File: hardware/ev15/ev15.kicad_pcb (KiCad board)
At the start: 4 copper layers, 94.4 x 80 mm, 165 parts, among them CN1 Conn_05x02_Female, CN2 PJ-242, J1 USB_C_Receptacle, J10 Conn_02x04_Odd_Even, J11 Conn_02x05_Counter_Clockwise, J2 Conn_01x02_Socket, J3 AudioJack4, J4 Conn_01x18_MountingPin, J5 Conn_02x03_Odd_Even, J7 Conn_02x05_Counter_Clockwise, J8 Conn_02x05_Counter_Clockwise, J9 Conn_02x05_Counter_Clockwise, Q1 2N7002, SW1 SW_SPDT, SW2 SW_Push, SW3 SW_Push, SW4 SW_Push, SW5 SW_Push, U1 BQ21040DBV, U10 STM32F405RGTx, U2 USBLC6-2P6, U3 STM32F072CBTx, U4 CH340C, U5 TPS63060, U6 WM8960CGEFL/RV, U7 ESP32-S3-WROOM-1, U8 M24C02-RMN6TP, U9 BM14B(0.8)-24DS-0.4V(53), Y1 Crystal_GND24

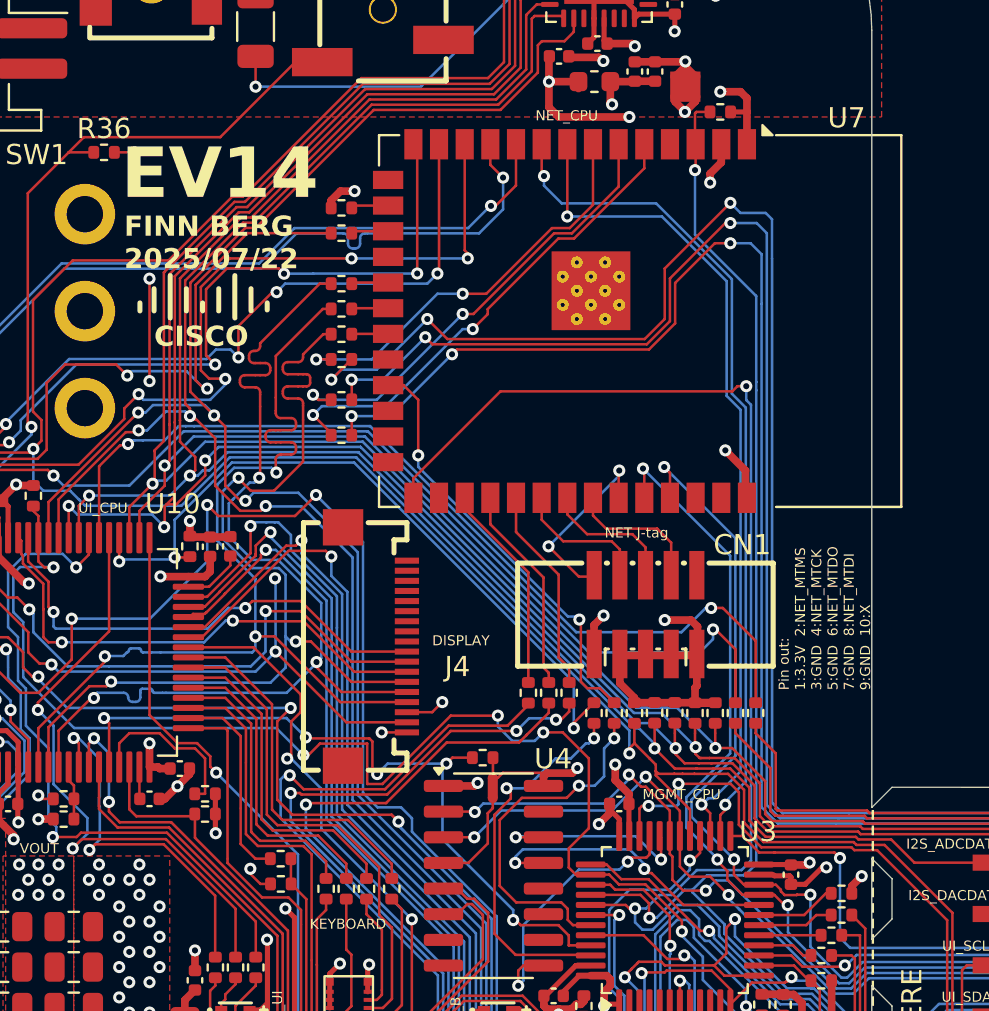
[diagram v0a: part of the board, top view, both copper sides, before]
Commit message: chore: renamed ev14a to ev15
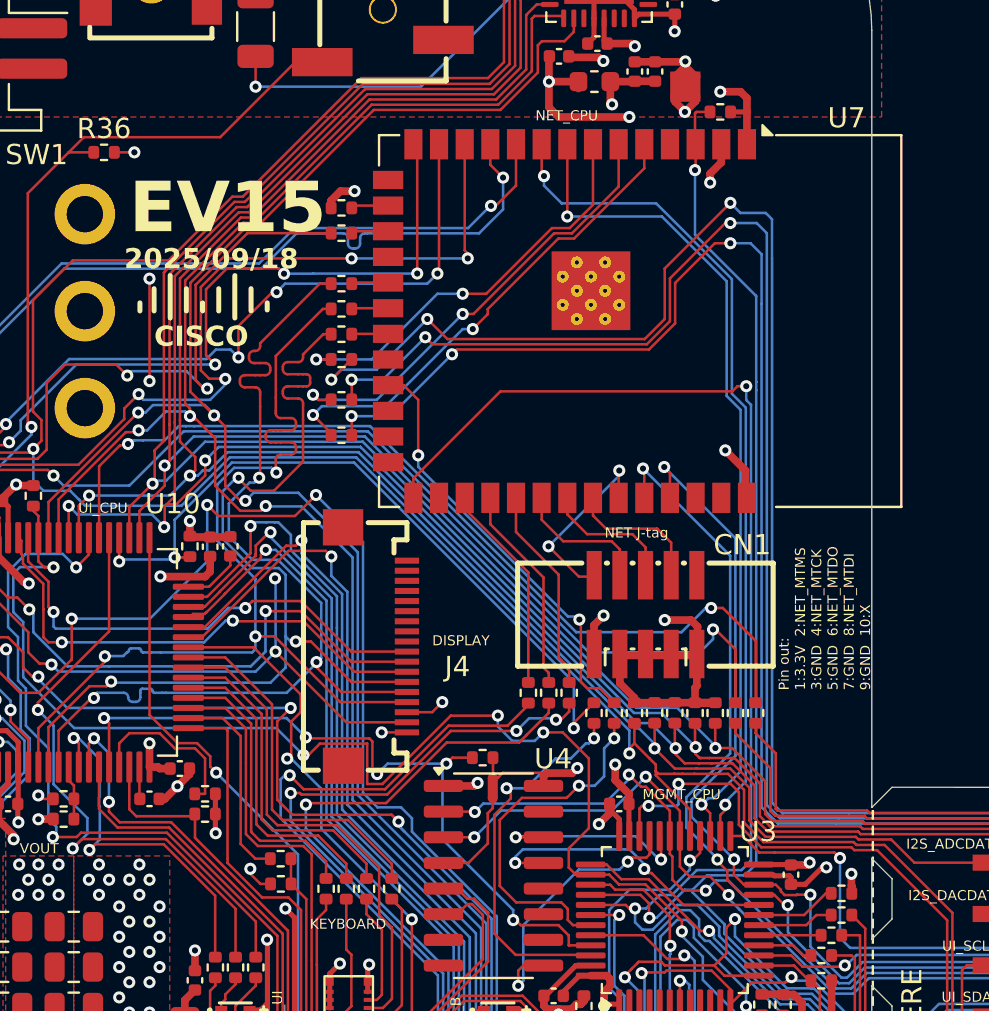
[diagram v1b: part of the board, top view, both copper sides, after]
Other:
- board text added: "2025/09/18"
- board text added: "EV15"
- board text removed: "EV14"
- board text removed: "FINN BERG 2025/07/22"
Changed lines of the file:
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@@
 		(title "Hactar PCB - Finn Berg, Brett Regnier")
 		(date "2025-07-25")
-		(rev "EV14")
+		(rev "EV15")
 		(company "CISCO SYSTEMS INC")
 	)
@@
 		)
 	)
-	(gr_text "EV14"
-		(at 187.11 71.55 0)
+	(gr_text "EV15"
+		(at 187.5 73.25 0)
 		(layer "F.SilkS")
 		(effects
@@
 		)
 	)
-	(gr_text "FINN BERG\n2025/07/22"
+	(gr_text "2025/09/18"
 		(at 187.25 74.9 0)
 		(layer "F.SilkS")
@@
 	)
 	(segment
-		(start 223.27 105.355)
-		(end 223.27 105.715)
-		(width 0.381)
-		(layer "F.Cu")
-		(net 4)
-	)
-	(segment
 		(start 215.53 66.52)
 		(end 215.01 67.04)
@@
 	)
 	(segment
+		(start 223.25 105.335)
+		(end 223.27 105.355)
+		(width 0.381)
+		(layer "F.Cu")
+		(net 4)
+	)
+	(segment
 		(start 218.01 86.07)
 		(end 218.08 86.14)
@@
 	)
 	(segment
+		(start 223.25 104.75)
+		(end 223.25 105.335)
+		(width 0.381)
+		(layer "F.Cu")
+		(net 4)
+	)
+	(segment
 		(start 212.51 96.28)
 		(end 212.51 96.04)
@@
 	)
 	(segment
+		(start 223.27 105.355)
+		(end 223.27 105.715)
+		(width 0.381)
+		(layer "F.Cu")
+		(net 4)
+	)
+	(segment
 		(start 250.51 112.246)
 		(end 250.4715 112.2845)
@@
 	)
 	(segment
-		(start 223.76 104.865)
-		(end 223.27 105.355)
-		(width 0.381)
-		(layer "F.Cu")
-		(net 4)
-	)
-	(segment
 		(start 198.848499 123.9715)
 		(end 200.01 122.809999)
@@
 	)
 	(via
-		(at 223.76 104.865)
+		(at 223.25 104.75)
 		(size 0.6)
 		(drill 0.3)
